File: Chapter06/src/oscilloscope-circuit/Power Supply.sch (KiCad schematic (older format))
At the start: 13 parts, among them U2 TLV75718PDBV, U3 MIC5501-3.0YM5, U4 LM2776, U5 TC59

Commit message: Working on chapter 6
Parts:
- U5: symbol Oscilloscope:TC59 -> Schematic_Symbols:TC59
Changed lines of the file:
@@
 	7350 3850 7350 3900
 $Comp
-L Oscilloscope:TC59 U5
+L Schematic_Symbols:TC59 U5
 U 1 1 5F6928A4
 P 7000 4500
@@
 	4250 4700 4000 4700
 $Comp
-L Oscilloscope:+3V0 #PWR031
+L Schematic_Symbols:+3V0 #PWR031
 U 1 1 5F6CAB3A
 P 4600 4500
@@
 	6700 4850 6700 5050
 $Comp
-L Oscilloscope:-3V0 #PWR033
+L Schematic_Symbols:-3V0 #PWR033
 U 1 1 5F750CB0
 P 5950 5250

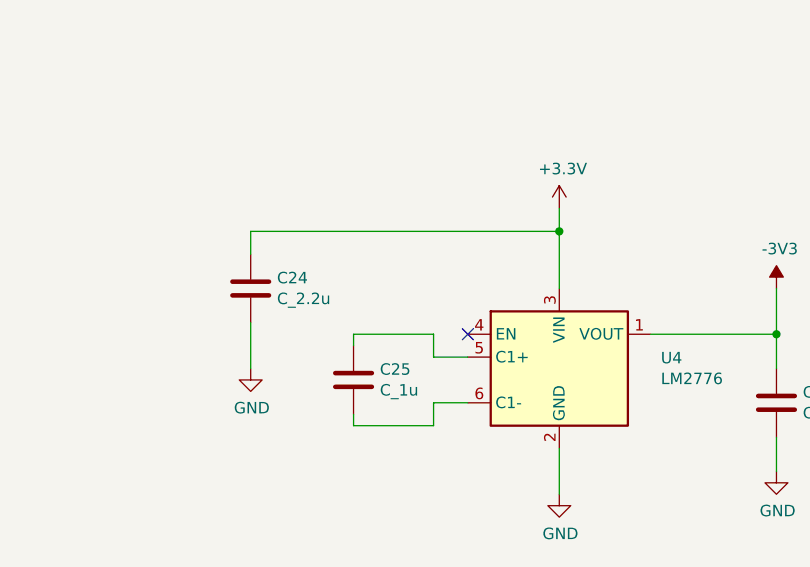
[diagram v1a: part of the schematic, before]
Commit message: Added chapters 9 and 10
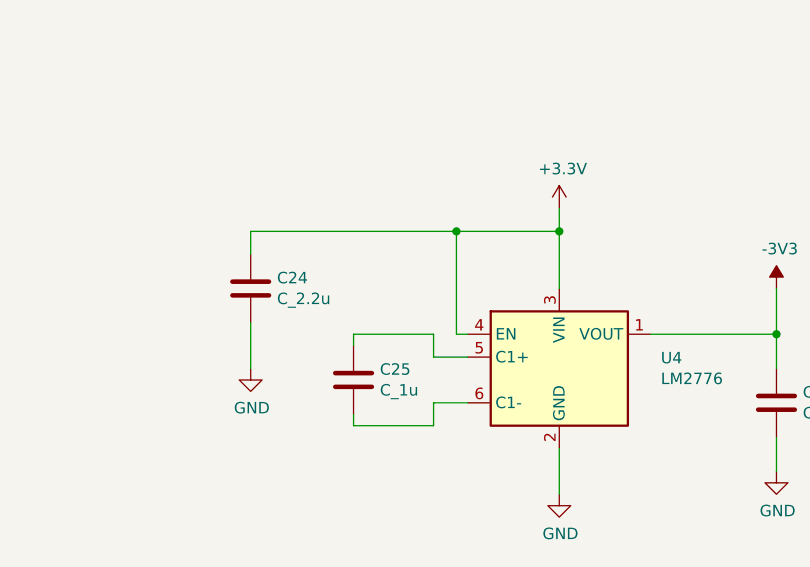
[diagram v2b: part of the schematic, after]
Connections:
- net +3V3: now also U4.4 (EN)
- no-connect marks 1 -> 0
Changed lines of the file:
@@
 	5650 2250 5650 2150
 Wire Wire Line
-	5650 2150 7000 2150
+	5650 2150 6550 2150
 Connection ~ 7000 2150
 Wire Wire Line
 	7000 2150 7000 2400
-NoConn ~ 6600 2600
 $Comp
 L Device:C C27
@@
 	1    0    0    -1
 $EndComp
+Wire Wire Line
+	6600 2600 6550 2600
+Wire Wire Line
+	6550 2600 6550 2150
+Connection ~ 6550 2150
+Wire Wire Line
+	6550 2150 7000 2150
 $EndSCHEMATC
